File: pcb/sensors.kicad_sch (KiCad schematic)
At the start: 19 parts, among them CON2 MIKROBUS_MODULECONN, U11 LIS2DH12, U12 LIS2MDLTR, U14 HL2304, U15 GXHTC3C

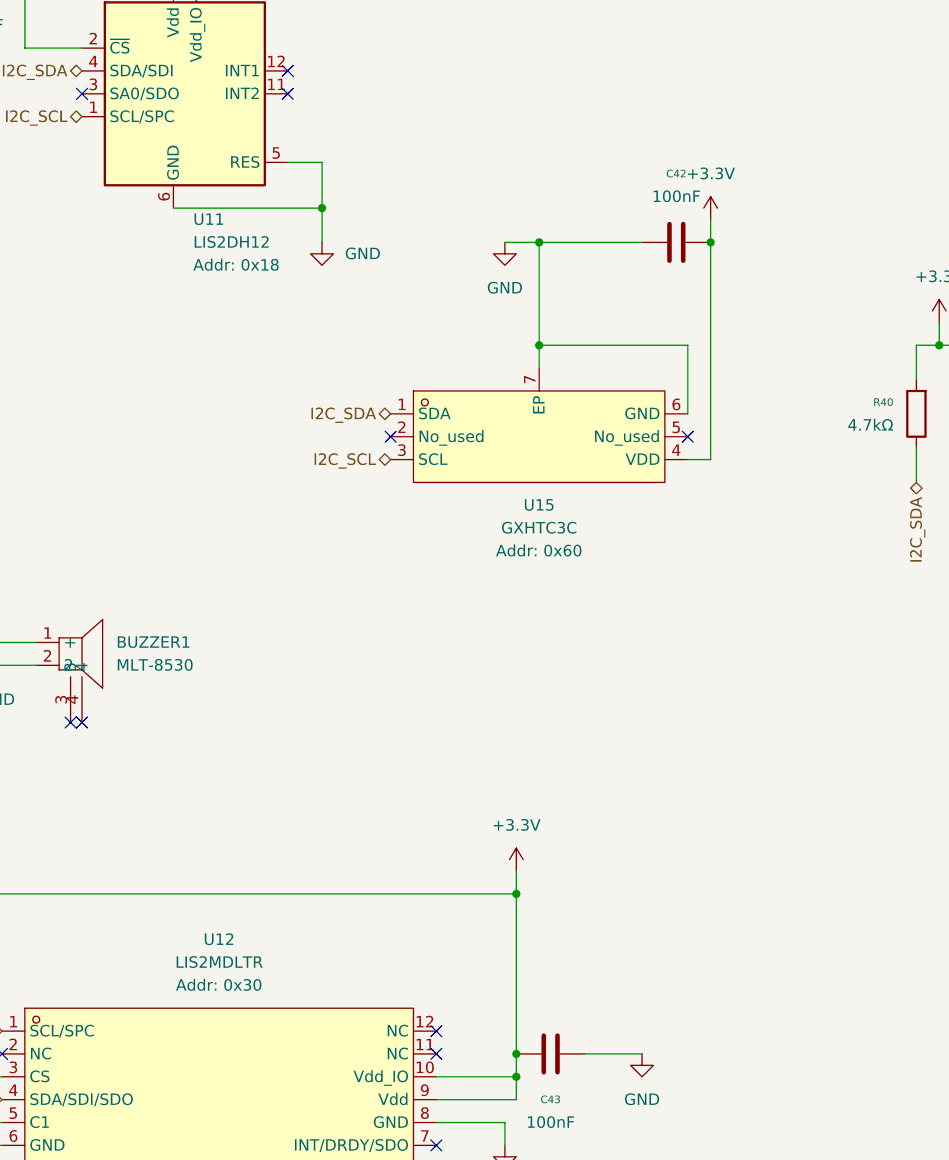
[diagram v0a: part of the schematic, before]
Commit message: fix GXHTC3C pinout
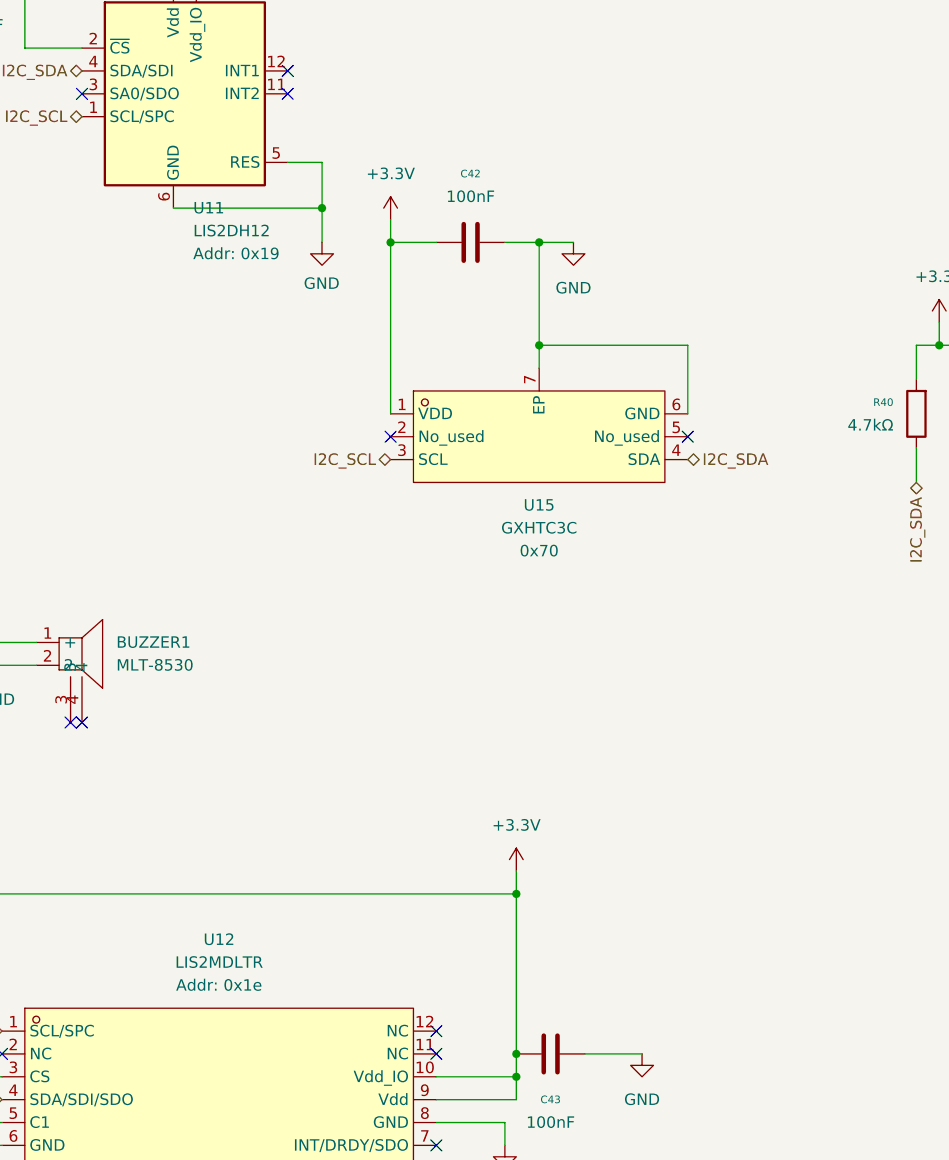
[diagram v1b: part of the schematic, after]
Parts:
- U11: Addr 0x18 -> 0x19
- U12: Addr 0x30 -> 0x1e
- U15: Addr 0x60 -> 0x70
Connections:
- net +3.3V: now also U15.1 (VDD); no longer U15.4 (VDD)
- net I2C_SDA: now also U15.4 (SDA); no longer U15.1 (SDA)
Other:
- moved on the sheet: C42
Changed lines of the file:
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@@
 	)
 	(junction
+		(at 160.02 62.23)
+		(diameter 0)
+		(color 0 0 0 0)
+	)
+	(junction
 		(at 250.19 24.13)
 		(diameter 0)
@@
 	)
 	(junction
-		(at 204.47 73.66)
+		(at 143.51 62.23)
 		(diameter 0)
 		(color 0 0 0 0)
 	)
 	(junction
-		(at 17.78 151.13)
+		(at 204.47 73.66)
 		(diameter 0)
 		(color 0 0 0 0)
 	)
 	(junction
-		(at 17.78 138.43)
+		(at 17.78 151.13)
 		(diameter 0)
 		(color 0 0 0 0)
 	)
 	(junction
-		(at 179.07 62.23)
+		(at 17.78 138.43)
 		(diameter 0)
 		(color 0 0 0 0)
@@
 	)
 	(junction
-		(at 160.02 62.23)
-		(diameter 0)
-		(color 0 0 0 0)
-	)
-	(junction
 		(at 119.38 30.48)
 		(diameter 0)
@@
 	(wire
 		(pts
-			(xy 176.53 86.36) (xy 179.07 86.36)
-		)
-		(stroke
-			(width 0)
-			(type default)
-		)
-	)
-	(wire
-		(pts
 			(xy 48.26 163.83) (xy 48.26 166.37)
 		)
@@
 	(wire
 		(pts
-			(xy 156.21 62.23) (xy 160.02 62.23)
-		)
-		(stroke
-			(width 0)
-			(type default)
-		)
-	)
-	(wire
-		(pts
 			(xy 207.01 73.66) (xy 207.01 77.47)
 		)
@@
 	(wire
 		(pts
-			(xy 160.02 62.23) (xy 171.45 62.23)
+			(xy 160.02 62.23) (xy 163.83 62.23)
 		)
 		(stroke
@@
 	(wire
 		(pts
+			(xy 143.51 81.28) (xy 143.51 62.23)
+		)
+		(stroke
+			(width 0)
+			(type default)
+		)
+	)
+	(wire
+		(pts
 			(xy 100.33 160.02) (xy 85.09 160.02)
 		)
@@
 	(wire
 		(pts
-			(xy 179.07 59.69) (xy 179.07 62.23)
+			(xy 143.51 59.69) (xy 143.51 62.23)
 		)
 		(stroke
@@
 	(wire
 		(pts
-			(xy 157.48 134.62) (xy 157.48 152.4)
+			(xy 143.51 62.23) (xy 148.59 62.23)
 		)
 		(stroke
@@
 	(wire
 		(pts
-			(xy 26.67 138.43) (xy 17.78 138.43)
+			(xy 157.48 134.62) (xy 157.48 152.4)
 		)
 		(stroke
@@
 	(wire
 		(pts
-			(xy 267.97 111.76) (xy 267.97 106.68)
+			(xy 26.67 138.43) (xy 17.78 138.43)
 		)
 		(stroke
@@
 	(wire
 		(pts
-			(xy 17.78 163.83) (xy 26.67 163.83)
+			(xy 267.97 111.76) (xy 267.97 106.68)
 		)
 		(stroke
@@
 	(wire
 		(pts
-			(xy 238.76 24.13) (xy 250.19 24.13)
+			(xy 17.78 163.83) (xy 26.67 163.83)
 		)
 		(stroke
@@
 	(wire
 		(pts
-			(xy 274.32 24.13) (xy 274.32 26.67)
+			(xy 238.76 24.13) (xy 250.19 24.13)
 		)
 		(stroke
@@
 	(wire
 		(pts
-			(xy 179.07 62.23) (xy 179.07 86.36)
+			(xy 274.32 24.13) (xy 274.32 26.67)
 		)
 		(stroke
@@
 	(wire
 		(pts
+			(xy 156.21 62.23) (xy 160.02 62.23)
+		)
+		(stroke
+			(width 0)
+			(type default)
+		)
+	)
+	(wire
+		(pts
 			(xy 160.02 62.23) (xy 160.02 73.66)
 		)
@@
 		)
 	)
-	(hierarchical_label "I2C_SDA"
-		(shape bidirectional)
-		(at 143.51 81.28 180)
-		(fields_autoplaced yes)
-		(effects
-			(font
-				(size 1.27 1.27)
-			)
-			(justify right)
-		)
-	)
 	(hierarchical_label "I2C_SCL"
 		(shape bidirectional)
@@
 		)
 	)
+	(hierarchical_label "I2C_SDA"
+		(shape bidirectional)
+		(at 176.53 86.36 0)
+		(fields_autoplaced yes)
+		(effects
+			(font
+				(size 1.27 1.27)
+			)
+			(justify left)
+		)
+	)
 	(hierarchical_label "SPI_SCK"
 		(shape bidirectional)
@@
 	(symbol
 		(lib_id "Device:C")
-		(at 175.26 62.23 90)
+		(at 152.4 62.23 270)
 		(unit 1)
 		(exclude_from_sim no)
@@
 		(fields_autoplaced yes)
 		(property "Reference" "C42"
-			(at 175.26 54.61 90)
+			(at 152.4 54.61 90)
 			(effects
 				(font
@@
 		)
 		(property "Value" "100nF"
-			(at 175.26 57.15 90)
+			(at 152.4 57.15 90)
 			(effects
 				(font
@@
 		)
 		(property "Footprint" "Capacitor_SMD:C_0603_1608Metric"
-			(at 179.07 61.2648 0)
+			(at 148.59 63.1952 0)
 			(effects
 				(font
@@
 		)
 		(property "Datasheet" "~"
-			(at 175.26 62.23 0)
+			(at 152.4 62.23 0)
 			(effects
 				(font
@@
 		)
 		(property "Description" "Unpolarized capacitor"
-			(at 175.26 62.23 0)
+			(at 152.4 62.23 0)
 			(effects
 				(font
@@
 		)
 		(property "LCSC" "C14663"
-			(at 172.72 64.77 0)
+			(at 154.94 59.69 0)
 			(effects
 				(font
@@
 		(fields_autoplaced yes)
 		(property "Reference" "U11"
-			(at 121.5741 59.69 0)
+			(at 121.5741 58.42 0)
 			(effects
 				(font
@@
 		)
 		(property "Value" "LIS2DH12"
-			(at 121.5741 62.23 0)
+			(at 121.5741 60.96 0)
 			(effects
 				(font
@@
 			)
 		)
-		(property "Addr" "0x18"
-			(at 121.5741 64.77 0)
+		(property "Addr" "0x19"
+			(at 121.5741 63.5 0)
 			(show_name yes)
 			(effects
@@
 		(on_board yes)
 		(dnp no)
-		(fields_autoplaced yes)
 		(property "Reference" "#PWR073"
 			(at 135.89 62.23 0)
@@
 		)
 		(property "Value" "GND"
-			(at 138.43 63.4999 0)
+			(at 133.858 66.802 0)
 			(effects
 				(font
@@
 	(symbol
 		(lib_id "power:+3.3V")
-		(at 179.07 59.69 0)
+		(at 143.51 59.69 0)
 		(unit 1)
 		(exclude_from_sim no)
@@
 		(fields_autoplaced yes)
 		(property "Reference" "#PWR079"
-			(at 179.07 63.5 0)
+			(at 143.51 63.5 0)
 			(effects
 				(font
@@
 		)
 		(property "Value" "+3.3V"
-			(at 179.07 54.61 0)
+			(at 143.51 54.61 0)
 			(effects
 				(font
@@
 		)
 		(property "Footprint" ""
-			(at 179.07 59.69 0)
+			(at 143.51 59.69 0)
 			(effects
 				(font
@@
 		)
 		(property "Datasheet" ""
-			(at 179.07 59.69 0)
+			(at 143.51 59.69 0)
 			(effects
 				(font
@@
 		)
 		(property "Description" "Power symbol creates a global label with name \"+3.3V\""
-			(at 179.07 59.69 0)
+			(at 143.51 59.69 0)
 			(effects
 				(font
@@
 	(symbol
 		(lib_id "power:GND")
-		(at 156.21 62.23 0)
+		(at 163.83 62.23 0)
 		(unit 1)
 		(exclude_from_sim no)
@@
 		(fields_autoplaced yes)
 		(property "Reference" "#PWR090"
-			(at 156.21 62.23 0)
+			(at 163.83 62.23 0)
 			(effects
 				(font
@@
 		)
 		(property "Value" "GND"
-			(at 156.21 67.31 0)
+			(at 163.83 67.31 0)
 			(effects
 				(font
@@
 		)
 		(property "Footprint" ""
-			(at 156.21 62.23 0)
+			(at 163.83 62.23 0)
 			(effects
 				(font
@@
 		)
 		(property "Datasheet" ""
-			(at 156.21 62.23 0)
+			(at 163.83 62.23 0)
 			(effects
 				(font
@@
 		)
 		(property "Description" "Power symbol creates a global label with name \"GND\" , ground"
-			(at 156.21 62.23 0)
+			(at 163.83 62.23 0)
 			(effects
 				(font
@@
 			)
 		)
-		(property "Addr" "0x60"
+		(property "Addr" "0x70"
 			(at 160.02 96.52 0)
-			(show_name yes)
 			(effects
 				(font
@@
 			)
 		)
-		(property "Addr" "0x30"
+		(property "Addr" "0x1e"
 			(at 124.46 144.78 0)
 			(show_name yes)

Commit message: review version
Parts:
- added C47: 100nF, Capacitor_SMD:C_0603_1608Metric, symbol Device:C
- added R46: 4.7kΩ, Resistor_SMD:R_0603_1608Metric, symbol Device:R
- added U13: HL2304, Package_TO_SOT_SMD:SOT-23, symbol Library:HL2304
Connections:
- net +3.3V: now also BUZZER1.1 (+), C47.1
- net ESP_IO2: now also R46.2; no longer BUZZER1.1 (+)
- net GND: now also C47.2, U13.2 (S); no longer BUZZER1.2
- new net: BUZZER1.2, U13.3 (D)
- new net: R46.1, U13.1 (G)
